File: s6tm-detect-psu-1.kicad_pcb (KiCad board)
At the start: 4 copper layers, 50 x 50 mm, 120 parts, among them J1 Conn_01x02, J2 Conn_01x02, J3 USB_C_Receptacle_USB2.0_14P, J4 Conn_01x04, J5 Conn_01x04, J6 Conn_01x04_Pin, J7 TC2030, SW1 SW_Push, SW2 SW_Push, U1 TPS259470x, U2 TPS259470x, U3 TPS259470x, U4 TPS62933, U5 TPS259470x, U6 SN65HVD230, U7 HT753-1, U8 STM32F103C8Tx, Y1 8M

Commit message: pcb: add crystal routing
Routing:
- net /Logic/XTAL_I: track 0.00 -> 10.4 mm
- net /Logic/XTAL_RO: track 0.00 -> 5.98 mm
- net /Logic/XTAL_O: track 0.00 -> 3.43 mm
- net GND: vias 84 -> 92
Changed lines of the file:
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@@
+	)
+	(via
+		(at 131.75 125.25)
+		(size 0.6)
+		(drill 0.3)
+		(layers "F.Cu" "B.Cu")
+		(free yes)
+		(net "GND")
+	)
+	(via
+		(at 133.5 125.25)
+		(size 0.6)
+		(drill 0.3)
+		(layers "F.Cu" "B.Cu")
+		(free yes)
+		(net "GND")
 	)
 	(via
@@
 	)
 	(via
+		(at 132 121)
+		(size 0.6)
+		(drill 0.3)
+		(layers "F.Cu" "B.Cu")
+		(free yes)
+		(net "GND")
+	)
+	(via
 		(at 121 111)
 		(size 0.7)
@@
 	)
 	(via
+		(at 135.25 125)
+		(size 0.6)
+		(drill 0.3)
+		(layers "F.Cu" "B.Cu")
+		(free yes)
+		(net "GND")
+	)
+	(via
 		(at 120.25 131.75)
 		(size 0.9)
@@
 	)
 	(via
+		(at 129 125.25)
+		(size 0.6)
+		(drill 0.3)
+		(layers "F.Cu" "B.Cu")
+		(free yes)
+		(net "GND")
+	)
+	(via
 		(at 113.25 152.25)
 		(size 0.9)
@@
 	)
 	(via
+		(at 127.25 125.25)
+		(size 0.6)
+		(drill 0.3)
+		(layers "F.Cu" "B.Cu")
+		(free yes)
+		(net "GND")
+	)
+	(via
 		(at 121.440867 122.253463)
 		(size 0.9)
@@
 	)
 	(via
+		(at 130.25 125.25)
+		(size 0.6)
+		(drill 0.3)
+		(layers "F.Cu" "B.Cu")
+		(free yes)
+		(net "GND")
+	)
+	(via
+		(at 129.25 120.75)
+		(size 0.6)
+		(drill 0.3)
+		(layers "F.Cu" "B.Cu")
+		(free yes)
+		(net "GND")
+	)
+	(via
 		(at 119 131.75)
 		(size 0.9)
@@
 		(net "GND")
 	)
+	(segment
+		(start 133.5 118)
+		(end 129.9 121.6)
+		(width 0.2)
+		(layer "F.Cu")
+		(net "/Logic/XTAL_I")
+	)
+	(segment
+		(start 133.5 116.9125)
+		(end 133.5 118)
+		(width 0.2)
+		(layer "F.Cu")
+		(net "/Logic/XTAL_I")
+	)
+	(segment
+		(start 129.9 121.6)
+		(end 129.9 123)
+		(width 0.2)
+		(layer "F.Cu")
+		(net "/Logic/XTAL_I")
+	)
+	(segment
+		(start 129.9 123.35)
+		(end 129.9 123)
+		(width 0.2)
+		(layer "F.Cu")
+		(net "/Logic/XTAL_I")
+	)
+	(segment
+		(start 127.75 124.025)
+		(end 129.225 124.025)
+		(width 0.2)
+		(layer "F.Cu")
+		(net "/Logic/XTAL_I")
+	)
+	(segment
+		(start 129.225 124.025)
+		(end 129.9 123.35)
+		(width 0.2)
+		(layer "F.Cu")
+		(net "/Logic/XTAL_I")
+	)
+	(segment
+		(start 133.175 119.325)
+		(end 134 118.5)
+		(width 0.2)
+		(layer "F.Cu")
+		(net "/Logic/XTAL_O")
+	)
+	(segment
+		(start 134 118.5)
+		(end 134 116.9125)
+		(width 0.2)
+		(layer "F.Cu")
+		(net "/Logic/XTAL_O")
+	)
+	(segment
+		(start 133.175 120)
+		(end 133.175 119.325)
+		(width 0.2)
+		(layer "F.Cu")
+		(net "/Logic/XTAL_O")
+	)
+	(segment
+		(start 133.6 123)
+		(end 134.375 123.775)
+		(width 0.2)
+		(layer "F.Cu")
+		(net "/Logic/XTAL_RO")
+	)
+	(segment
+		(start 134.825 120)
+		(end 133.6 121.225)
+		(width 0.2)
+		(layer "F.Cu")
+		(net "/Logic/XTAL_RO")
+	)
+	(segment
+		(start 133.6 121.225)
+		(end 133.6 123)
+		(width 0.2)
+		(layer "F.Cu")
+		(net "/Logic/XTAL_RO")
+	)
+	(segment
+		(start 134.375 123.775)
+		(end 135.75 123.775)
+		(width 0.2)
+		(layer "F.Cu")
+		(net "/Logic/XTAL_RO")
+	)
 	(zone

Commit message: pcb: add swd routing
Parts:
- turned D13 to 180 degrees
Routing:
- net /Logic/SWO: track 0.00 -> 10.8 mm
- net /Logic/SWDIO: track 0.00 -> 10.3 mm
- net /Logic/SWCLK: track 0.00 -> 9.78 mm
- net /Logic/NRST: track 0.00 -> 7.65 mm
- net +3V3: track 0.00 -> 3.10 mm
- net GND: vias 92 -> 91

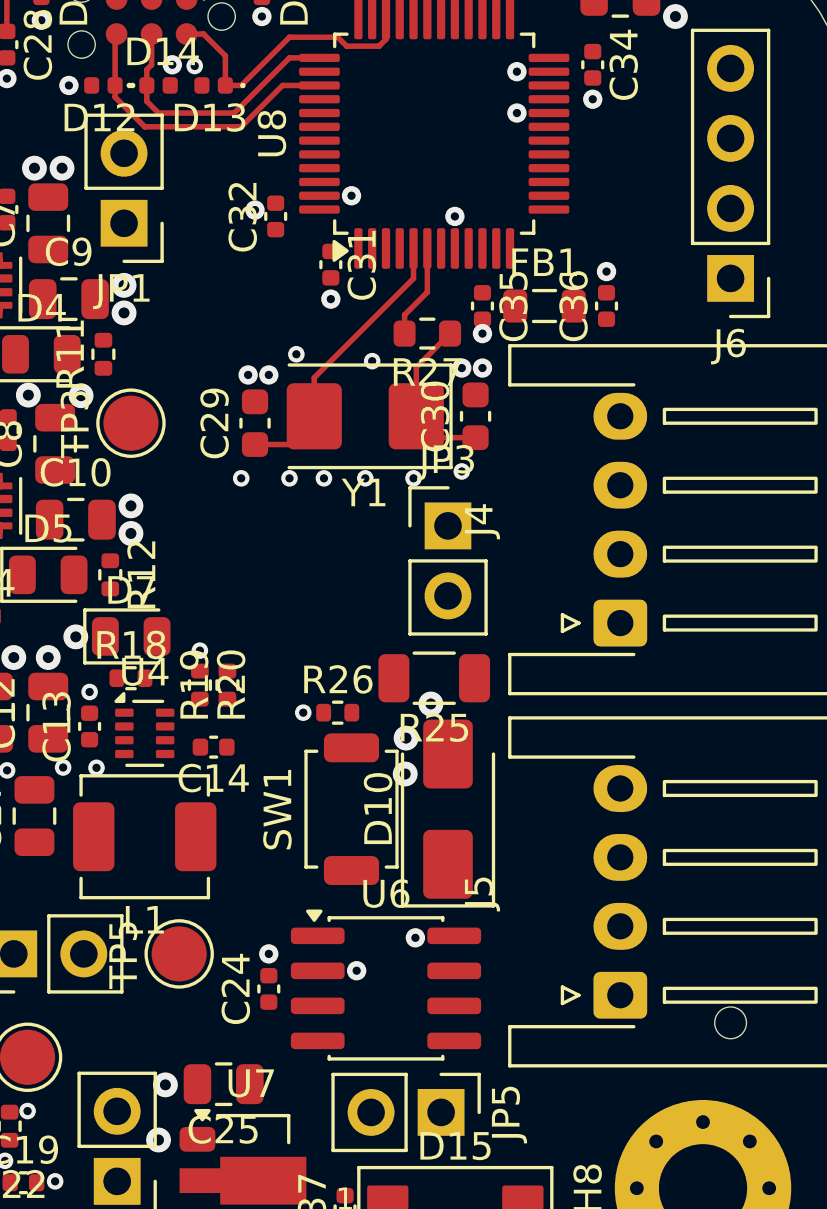
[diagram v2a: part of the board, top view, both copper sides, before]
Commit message: pcb: add can routing
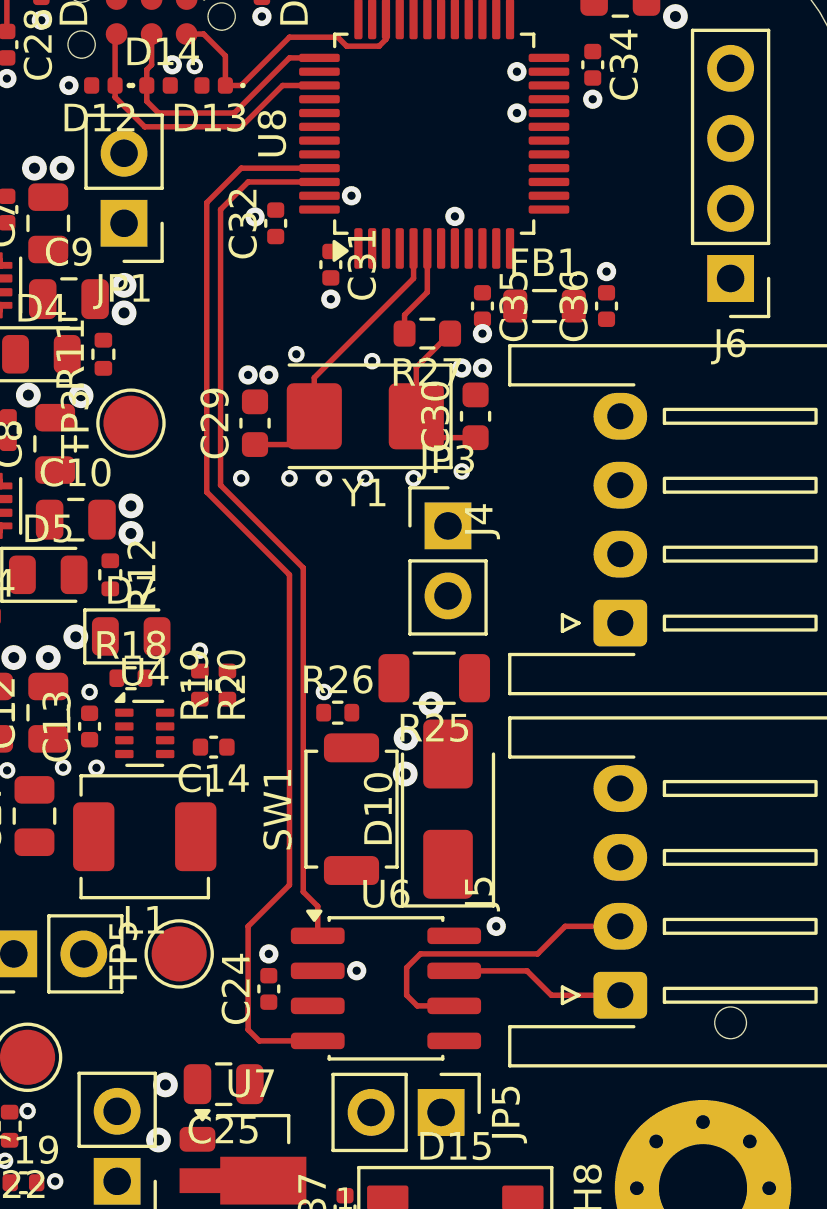
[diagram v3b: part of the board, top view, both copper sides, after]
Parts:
- moved C32 0.25 mm to (128.5, 116.0)
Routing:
- net /Logic/CAN_RX: track 0.00 -> 39.2 mm
- net /Logic/CAN_TX: track 0.00 -> 31.8 mm
- net /Logic/CANL: track 0.00 -> 11.3 mm
- net /Logic/CANH: track 0.00 -> 6.39 mm
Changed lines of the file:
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@@
 	(footprint "Capacitor_SMD:C_0402_1005Metric"
 		(layer "F.Cu")
-		(at 128.5 115.75 90)
+		(at 128.5 116 90)
 		(descr "Capacitor SMD 0402 (1005 Metric), square (rectangular) end terminal, IPC-7351 nominal, (Body size source: IPC-SM-782 page 76, https://www.pcb-3d.com/wordpress/wp-content/uploads/ipc-sm-782a_amendment_1_and_2.pdf)")
 		(tags "capacitor")
@@
 	)
 	(via
-		(at 133.567662 141.916904)
+		(at 136.5 141.5)
 		(size 0.7)
 		(drill 0.3)
@@
 	)
 	(via
-		(at 127.75 115.52)
+		(at 127.75 115.77)
 		(size 0.7)
 		(drill 0.3)
@@
 	)
 	(via
-		(at 129.5 133.75)
+		(at 130.25 133)
 		(size 0.6)
 		(drill 0.3)
@@
 	)
 	(segment
+		(start 130.025 145.655)
+		(end 127.905 145.655)
+		(width 0.2)
+		(layer "F.Cu")
+		(net "/Logic/CAN_RX")
+	)
+	(segment
+		(start 129 140)
+		(end 129 128.75)
+		(width 0.2)
+		(layer "F.Cu")
+		(net "/Logic/CAN_RX")
+	)
+	(segment
+		(start 127.5 141.5)
+		(end 129 140)
+		(width 0.2)
+		(layer "F.Cu")
+		(net "/Logic/CAN_RX")
+	)
+	(segment
+		(start 126 125.75)
+		(end 126 115.25)
+		(width 0.2)
+		(layer "F.Cu")
+		(net "/Logic/CAN_RX")
+	)
+	(segment
+		(start 127.905 145.655)
+		(end 127.5 145.25)
+		(width 0.2)
+		(layer "F.Cu")
+		(net "/Logic/CAN_RX")
+	)
+	(segment
+		(start 126 115.25)
+		(end 127.25 114)
+		(width 0.2)
+		(layer "F.Cu")
+		(net "/Logic/CAN_RX")
+	)
+	(segment
+		(start 127.25 114)
+		(end 130.0875 114)
+		(width 0.2)
+		(layer "F.Cu")
+		(net "/Logic/CAN_RX")
+	)
+	(segment
+		(start 129 128.75)
+		(end 126 125.75)
+		(width 0.2)
+		(layer "F.Cu")
+		(net "/Logic/CAN_RX")
+	)
+	(segment
+		(start 127.5 145.25)
+		(end 127.5 141.5)
+		(width 0.2)
+		(layer "F.Cu")
+		(net "/Logic/CAN_RX")
+	)
+	(segment
+		(start 126.5 115.5)
+		(end 126.5 125.5)
+		(width 0.2)
+		(layer "F.Cu")
+		(net "/Logic/CAN_TX")
+	)
+	(segment
+		(start 129.5 140.25)
+		(end 130.025 140.775)
+		(width 0.2)
+		(layer "F.Cu")
+		(net "/Logic/CAN_TX")
+	)
+	(segment
+		(start 127.5 114.5)
+		(end 126.5 115.5)
+		(width 0.2)
+		(layer "F.Cu")
+		(net "/Logic/CAN_TX")
+	)
+	(segment
+		(start 130.025 140.775)
+		(end 130.025 141.845)
+		(width 0.2)
+		(layer "F.Cu")
+		(net "/Logic/CAN_TX")
+	)
+	(segment
+		(start 129.5 128.5)
+		(end 129.5 140.25)
+		(width 0.2)
+		(layer "F.Cu")
+		(net "/Logic/CAN_TX")
+	)
+	(segment
+		(start 130.0875 114.5)
+		(end 127.5 114.5)
+		(width 0.2)
+		(layer "F.Cu")
+		(net "/Logic/CAN_TX")
+	)
+	(segment
+		(start 126.5 125.5)
+		(end 129.5 128.5)
+		(width 0.2)
+		(layer "F.Cu")
+		(net "/Logic/CAN_TX")
+	)
+	(segment
 		(start 133.6 123)
 		(end 134.375 123.775)
@@
 		(net "/Logic/XTAL_RO")
 	)
+	(segment
+		(start 137.615 143.115)
+		(end 134.975 143.115)
+		(width 0.2)
+		(layer "F.Cu")
+		(net "/Logic/CANH")
+	)
+	(segment
+		(start 141 144)
+		(end 138.5 144)
+		(width 0.2)
+		(layer "F.Cu")
+		(net "/Logic/CANH")
+	)
+	(segment
+		(start 138.5 144)
+		(end 137.615 143.115)
+		(width 0.2)
+		(layer "F.Cu")
+		(net "/Logic/CANH")
+	)
+	(segment
+		(start 138 142.5)
+		(end 139 141.5)
+		(width 0.2)
+		(layer "F.Cu")
+		(net "/Logic/CANL")
+	)
+	(segment
+		(start 133.635 144.385)
+		(end 133.25 144)
+		(width 0.2)
+		(layer "F.Cu")
+		(net "/Logic/CANL")
+	)
+	(segment
+		(start 133.75 142.5)
+		(end 138 142.5)
+		(width 0.2)
+		(layer "F.Cu")
+		(net "/Logic/CANL")
+	)
+	(segment
+		(start 139 141.5)
+		(end 141 141.5)
+		(width 0.2)
+		(layer "F.Cu")
+		(net "/Logic/CANL")
+	)
+	(segment
+		(start 133.25 144)
+		(end 133.25 143)
+		(width 0.2)
+		(layer "F.Cu")
+		(net "/Logic/CANL")
+	)
+	(segment
+		(start 133.25 143)
+		(end 133.75 142.5)
+		(width 0.2)
+		(layer "F.Cu")
+		(net "/Logic/CANL")
+	)
+	(segment
+		(start 134.975 144.385)
+		(end 133.635 144.385)
+		(width 0.2)
+		(layer "F.Cu")
+		(net "/Logic/CANL")
+	)
 	(zone

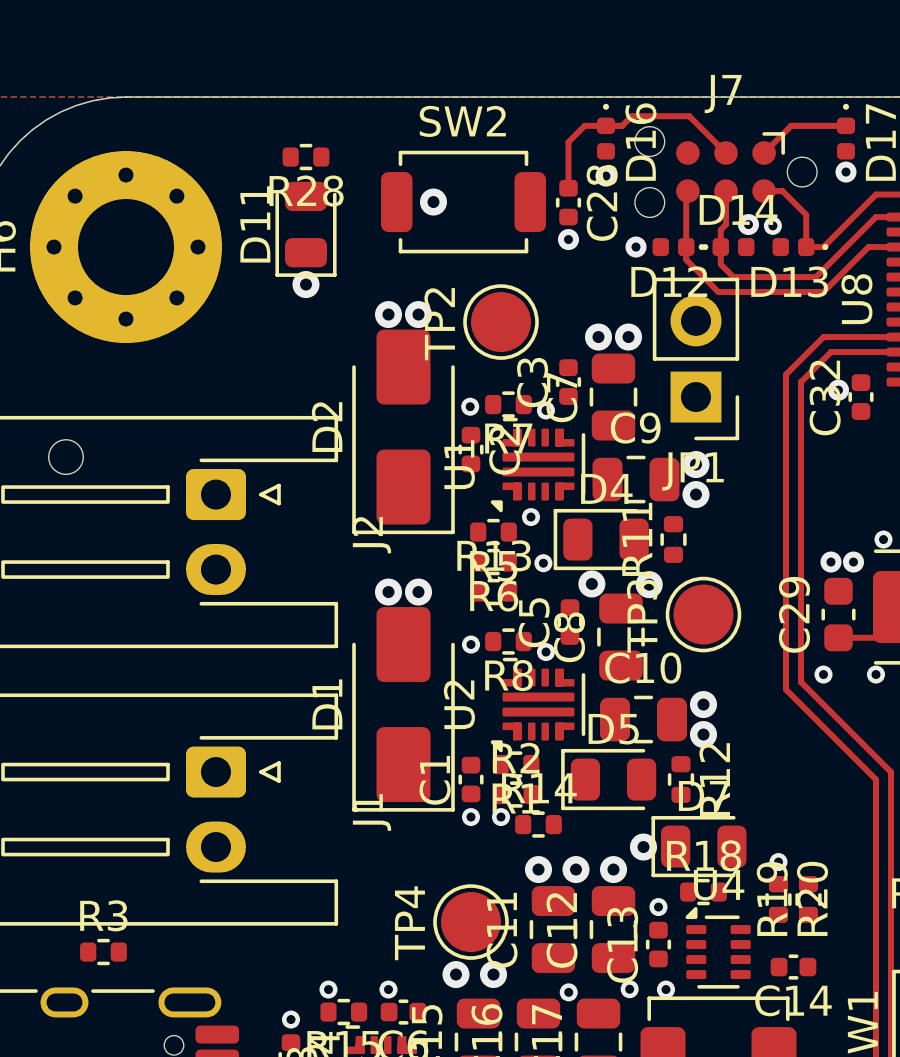
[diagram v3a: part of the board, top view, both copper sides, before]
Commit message: pcb: add batt efuses routing
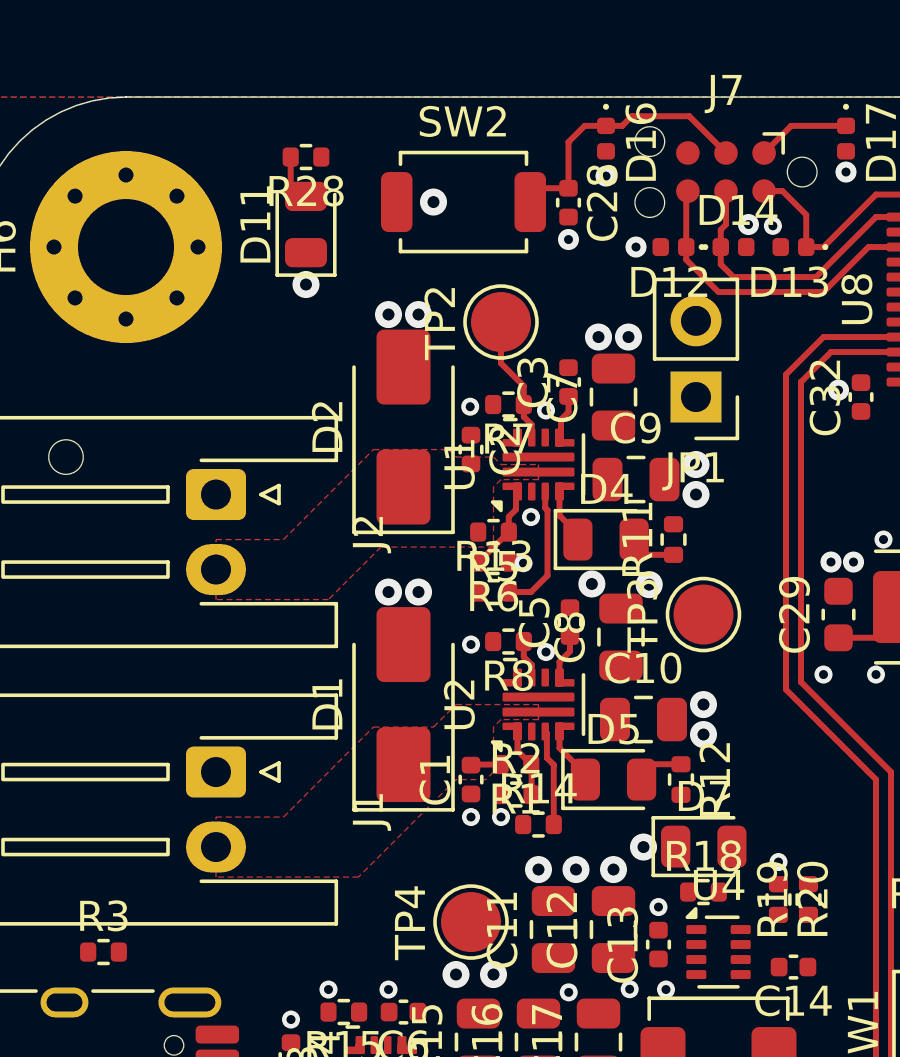
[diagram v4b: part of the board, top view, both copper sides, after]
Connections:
- U2 pad 2: IN2 -> IN1
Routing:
- net IN1: track 0.00 -> 4.34 mm
- net ILM1: track 0.00 -> 4.27 mm
- net IN2: track 0.00 -> 3.22 mm
- net BATT1_V: track 0.00 -> 2.90 mm
- net BATT2_V: track 0.00 -> 2.29 mm
- net Net-(D5-K): track 0.00 -> 1.96 mm
- net Net-(D4-K): track 0.00 -> 1.85 mm
- net Net-(D4-A): track 0.00 -> 1.63 mm
- net Net-(D11-A): track 0.00 -> 1.63 mm
- net Net-(D5-A): track 0.00 -> 1.63 mm
- net Net-(U1-DVDT): track 0.00 -> 1.62 mm
- net Net-(U2-DVDT): track 0.00 -> 1.51 mm
- net /Logic/NRST: track 7.65 -> 9.12 mm
- net ILM2: track 0.00 -> 1.31 mm
- net Net-(D1-A1): track 0.00 -> 1.00 mm
- added copper zone on F.Cu, net Net-(D1-A1)
- added copper zone on F.Cu, net Net-(D2-A1)

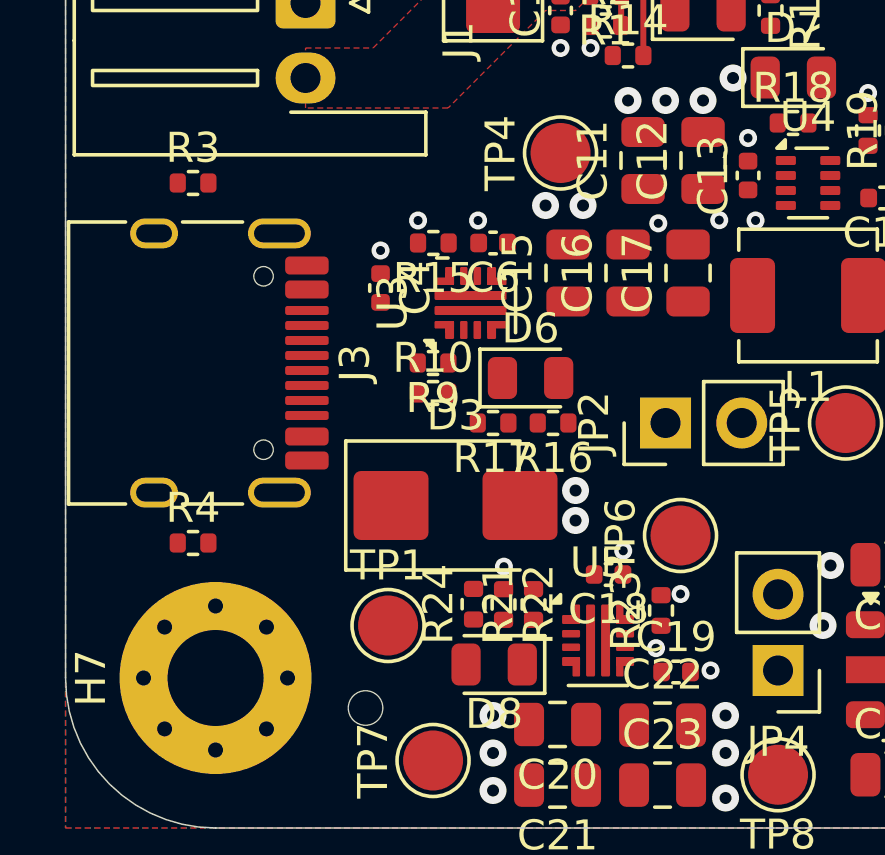
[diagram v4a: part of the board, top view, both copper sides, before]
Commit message: pcb: add +5V efuse routing
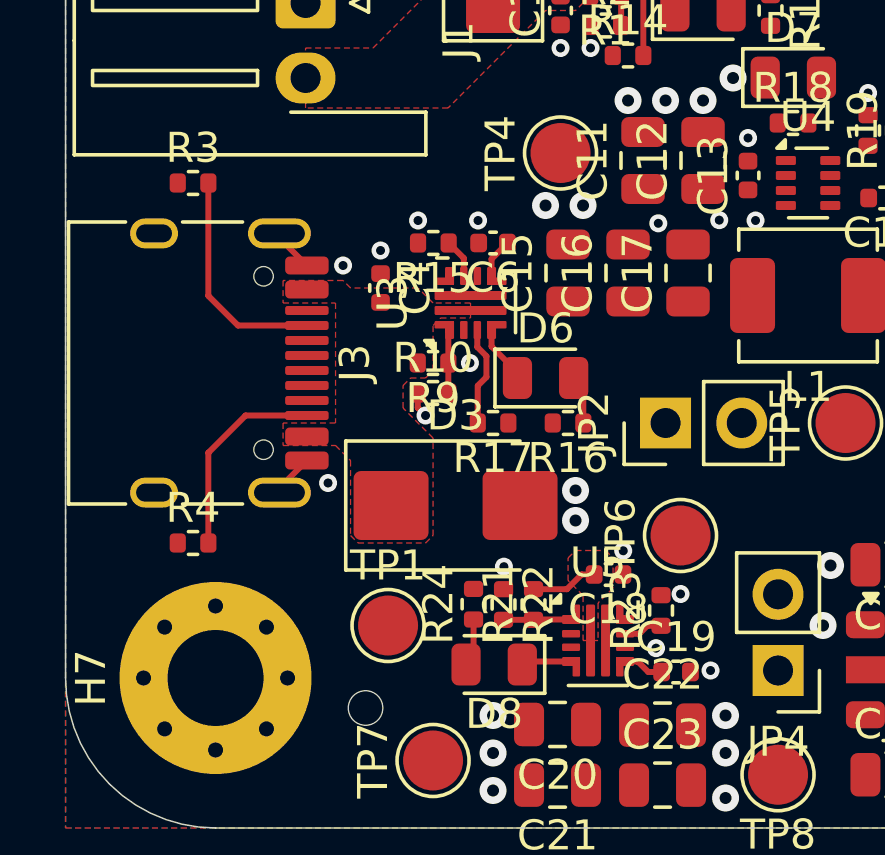
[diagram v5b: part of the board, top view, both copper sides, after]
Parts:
- moved D6 0.50 mm to (115.0, 141.0)
- moved R16 0.50 mm to (115.8, 142.5)
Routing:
- net Net-(J3-CC1): track 0.00 -> 7.46 mm
- net Net-(J3-CC2): track 0.00 -> 6.81 mm
- net GND: track 0.00 -> 3.76 mm, vias 91 -> 95
- net IN3: track 0.00 -> 3.35 mm
- net 5_V: track 0.00 -> 2.25 mm
- net +5V_SMPS: track 0.00 -> 2.22 mm
- net Net-(U3-EN/UVLO): track 0.00 -> 2.12 mm
- net Net-(D6-K): track 0.00 -> 1.96 mm
- net Net-(D8-K): track 0.00 -> 1.67 mm
- net Net-(D6-A): track 0.00 -> 1.63 mm
- net Net-(D8-A): track 0.00 -> 1.60 mm
- net Net-(U5-DVDT): track 0.00 -> 1.36 mm
- net Net-(U3-DVDT): track 0.00 -> 1.32 mm
- net ILM4: track 0.00 -> 1.31 mm
- net ILM3: track 0.00 -> 1.31 mm
- added copper zone on F.Cu, net +5V_SMPS
- added copper zone on F.Cu, net +Vbus

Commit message: pcb: add v and i routing
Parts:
- moved R1 0.50 mm to (117.0, 128.8)
- moved R14 0.50 mm to (117.8, 130.8)
- moved R2 0.50 mm to (117.0, 129.8)
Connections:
- U8 pad 10: ILM1 -> ILM4
- U8 pad 11: ILM2 -> ILM3
- U8 pad 14: BATT1_V -> 5_V
- U8 pad 16: 5_V -> BATT1_V
- U8 pad 18: ILM3 -> ILM2
- U8 pad 19: ILM4 -> ILM1
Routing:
- net BATT2_V: track 2.29 -> 55.2 mm, vias 0 -> 2
- net BATT1_V: track 2.90 -> 40.4 mm, vias 0 -> 2
- net ILM2: track 1.31 -> 31.3 mm, vias 0 -> 2
- net ILM1: track 4.27 -> 28.3 mm, vias 0 -> 2
- net IN1: track 4.34 -> 20.1 mm, vias 0 -> 3
- net IN2: track 3.22 -> 3.72 mm
- net GND: vias 95 -> 98
